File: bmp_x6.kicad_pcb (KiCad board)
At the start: 2 copper layers, 50 x 50 mm, 67 parts, among them J1 USB_B, J2 Conn_01x05_Pin, J3 Conn_02x05_Odd_Even, Q1 NMOS, Q2 PMOS, Q3 PMOS, Q4 NMOS, SW1 SW_Push, U1 STM32F103CBTx, U2 USB6B1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

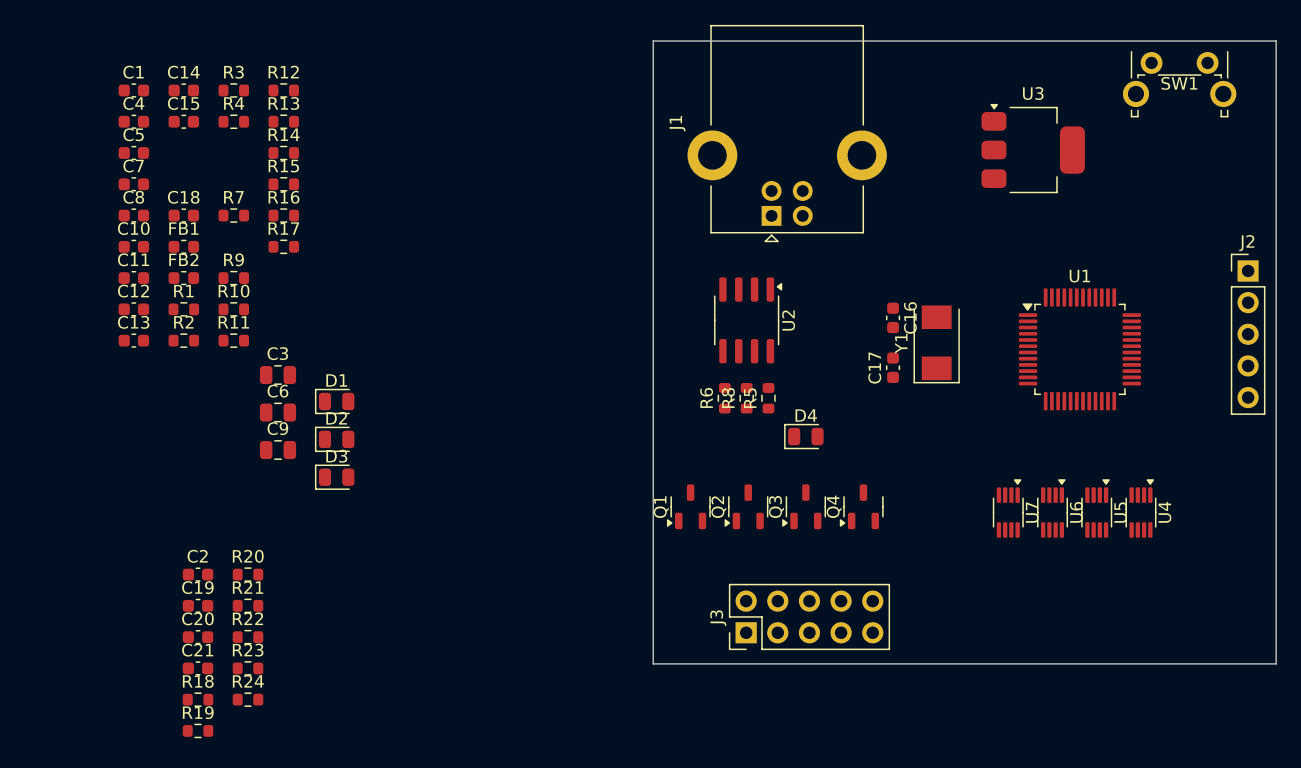
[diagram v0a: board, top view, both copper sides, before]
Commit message: pcb components relocated.
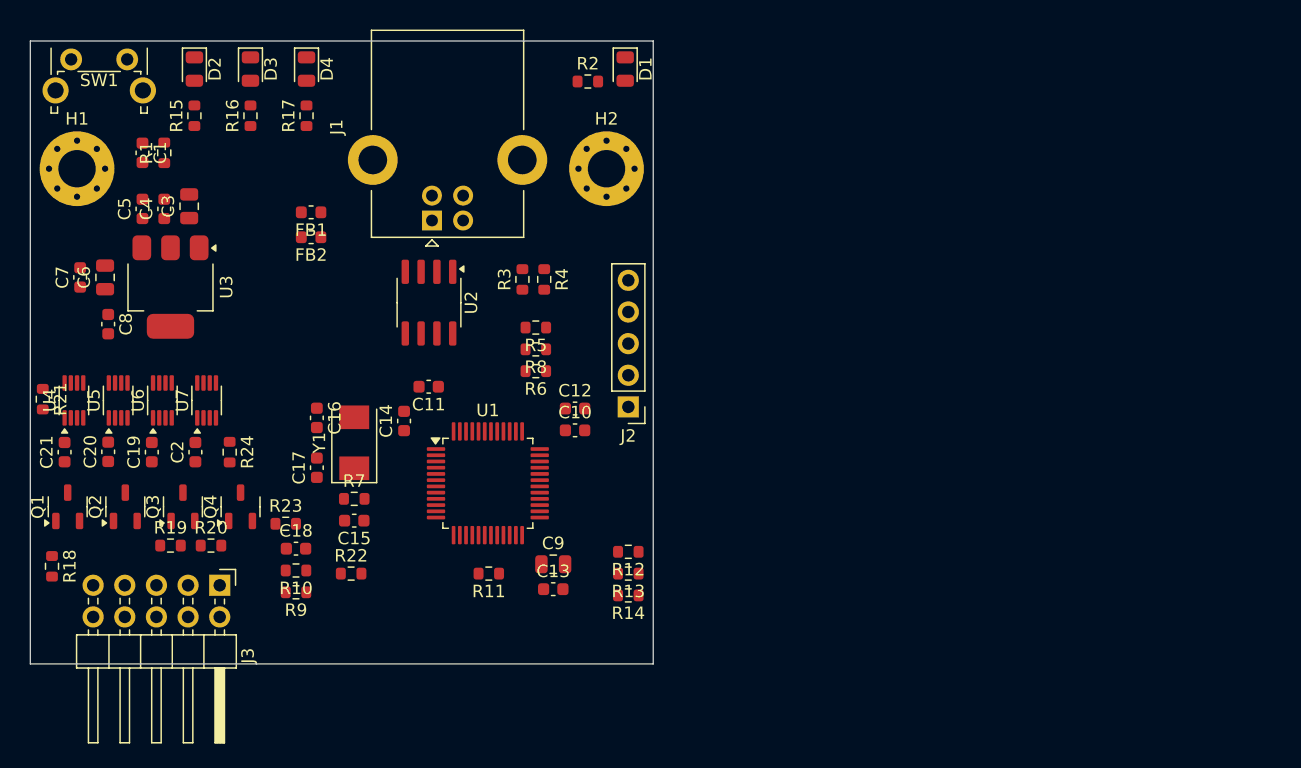
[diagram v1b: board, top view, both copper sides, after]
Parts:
- added H1: MountingHole, MountingHole:MountingHole_3mm_Pad_Via, F.Cu at (29.0, 30.0)
- added H2: MountingHole, MountingHole:MountingHole_3mm_Pad_Via, F.Cu at (71.5, 30.0)
- J3: footprint Connector_PinHeader_2.54mm:PinHeader_2x05_P2.54mm_Vertical -> Connector_PinHeader_2.54mm:PinHeader_2x05_P2.54mm_Horizontal
- moved SW1 86.7 mm to (28.5, 21.2)
- moved U4 86.1 mm to (28.8, 48.6), turned to 90 degrees
- moved U5 79.1 mm to (32.3, 48.6), turned to 90 degrees
- moved U6 72.0 mm to (35.9, 48.6), turned to 90 degrees
- moved U3 70.1 mm to (36.5, 39.5), turned to -90 degrees
- moved U7 65.0 mm to (39.4, 48.6), turned to 90 degrees
- moved J2 50.9 mm to (73.2, 49.1), turned to 180 degrees
- moved Q1 50.0 mm to (28.2, 57.1)
- moved Q2 50.0 mm to (32.9, 57.1)
- moved Q3 50.0 mm to (37.5, 57.1)
- moved Q4 50.0 mm to (42.1, 57.1)
- moved D4 49.8 mm to (47.4, 22.0), turned to -90 degrees
- moved U1 48.7 mm to (62.0, 55.2)
- moved Y1 47.4 mm to (51.2, 52.0)
- moved C16 46.9 mm to (48.2, 50.0)
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
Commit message: pcb drawing try
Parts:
- moved R5 3.77 mm to (63.0, 45.2)
- moved R8 2.97 mm to (63.0, 43.7)
- moved R6 2.91 mm to (63.0, 46.8)
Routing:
- net /mcu/VER_2: track 0.00 -> 20.9 mm, vias 0 -> 2
- net /mcu/VER_1: track 0.00 -> 18.8 mm, vias 0 -> 2
- net +3.3V: track 0.00 -> 18.6 mm
- net /mcu/VER_0: track 0.00 -> 16.5 mm, vias 0 -> 2
- net Net-(U1-PD0): track 0.00 -> 13.6 mm
- net /mcu/OWN_SWCLK: track 0.00 -> 13.3 mm
- net /mcu/OWN_SWDIO: track 0.00 -> 13.0 mm
- net /mcu/USBX2_DM: track 0.00 -> 12.3 mm
- net /mcu/USBX2_DP: track 0.00 -> 12.1 mm
- net /mcu/USBX1_DP: track 0.00 -> 11.6 mm, vias 0 -> 2
- net /mcu/USBX1_DM: track 0.00 -> 11.1 mm, vias 0 -> 2
- net Net-(U1-PD1): track 0.00 -> 10.3 mm
